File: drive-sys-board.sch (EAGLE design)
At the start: 34 parts

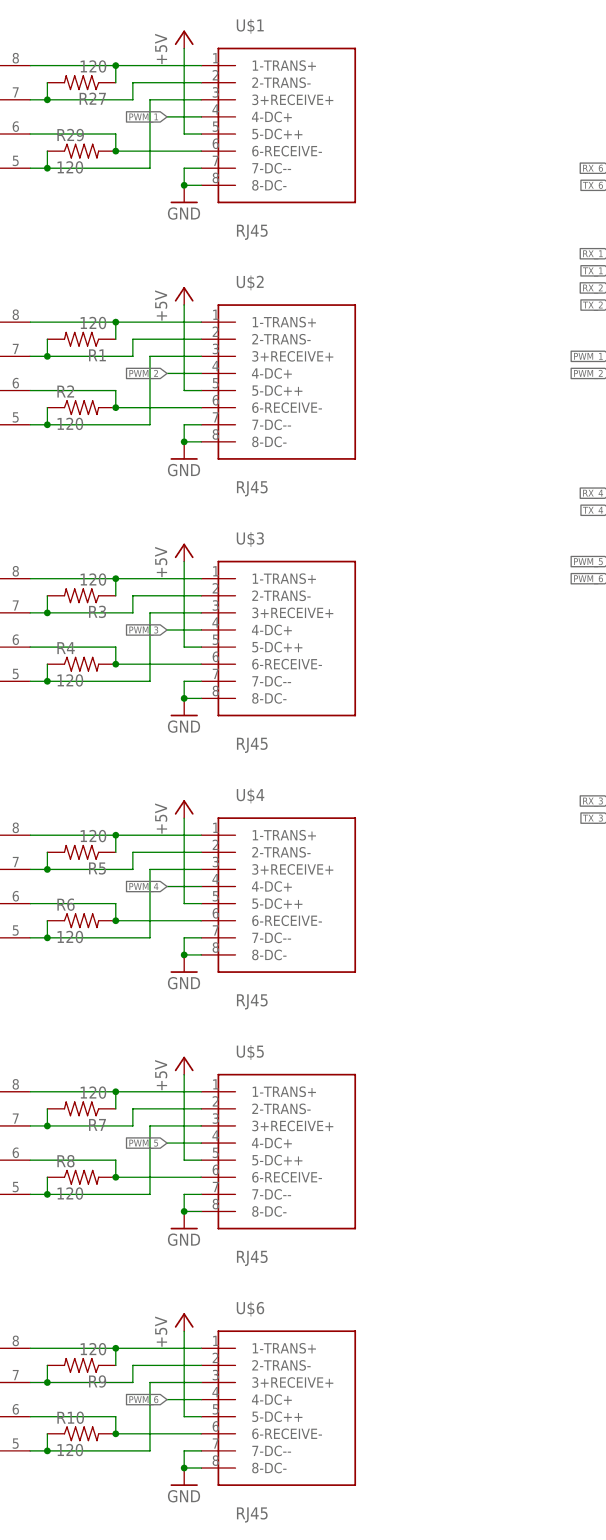
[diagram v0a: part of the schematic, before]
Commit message: changed rj45 conn
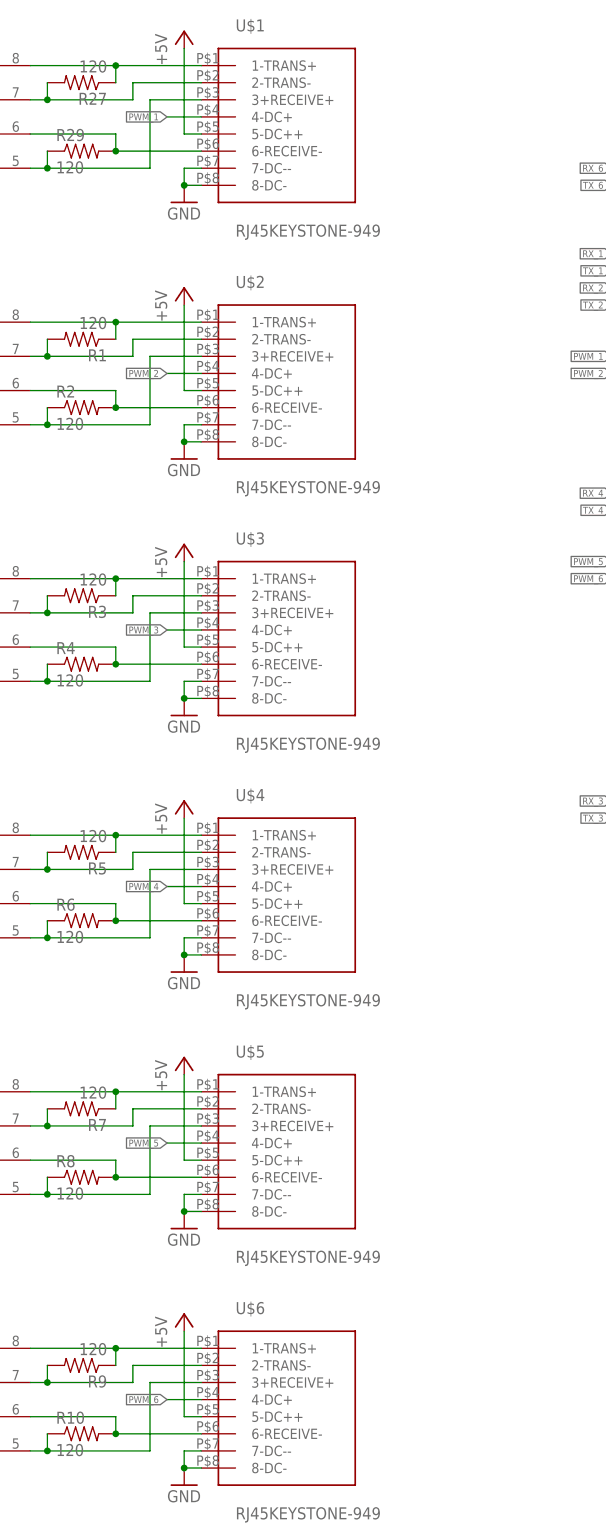
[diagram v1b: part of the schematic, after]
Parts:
- U$1, U$2, U$3, U$4, U$5, U$6: value RJ45 -> RJ45KEYSTONE-949; device MRDT-2014-All:RJ45 -> MRDT-2015-General:RJ45KEYSTONE-949
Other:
- moved on the sheet: U$1, U$2, U$3, U$4, U$5, U$6
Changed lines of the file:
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@@
 <part name="C1" library="SparkFun-Passives" deviceset="CAP" device="1206" value="0.1uF"/>
 <part name="GND13" library="supply1" deviceset="GND" device=""/>
-<part name="U$1" library="MRDT-2014-All" deviceset="RJ45" device=""/>
+<part name="U$1" library="MRDT-2015-General" deviceset="RJ45" device="KEYSTONE-949" value="RJ45KEYSTONE-949"/>
 <part name="GND1" library="supply1" deviceset="GND" device=""/>
 <part name="P+1" library="supply1" deviceset="+5V" device=""/>
@@
 <part name="C2" library="SparkFun-Passives" deviceset="CAP" device="1206" value="0.1uF"/>
 <part name="GND3" library="supply1" deviceset="GND" device=""/>
-<part name="U$2" library="MRDT-2014-All" deviceset="RJ45" device=""/>
+<part name="U$2" library="MRDT-2015-General" deviceset="RJ45" device="KEYSTONE-949"/>
 <part name="GND4" library="supply1" deviceset="GND" device=""/>
 <part name="P+3" library="supply1" deviceset="+5V" device=""/>
@@
 <part name="C3" library="SparkFun-Passives" deviceset="CAP" device="1206" value="0.1uF"/>
 <part name="GND6" library="supply1" deviceset="GND" device=""/>
-<part name="U$3" library="MRDT-2014-All" deviceset="RJ45" device=""/>
+<part name="U$3" library="MRDT-2015-General" deviceset="RJ45" device="KEYSTONE-949"/>
 <part name="GND7" library="supply1" deviceset="GND" device=""/>
 <part name="P+5" library="supply1" deviceset="+5V" device=""/>
@@
 <part name="C4" library="SparkFun-Passives" deviceset="CAP" device="1206" value="0.1uF"/>
 <part name="GND9" library="supply1" deviceset="GND" device=""/>
-<part name="U$4" library="MRDT-2014-All" deviceset="RJ45" device=""/>
+<part name="U$4" library="MRDT-2015-General" deviceset="RJ45" device="KEYSTONE-949"/>
 <part name="GND10" library="supply1" deviceset="GND" device=""/>
 <part name="P+7" library="supply1" deviceset="+5V" device=""/>
@@
 <part name="C5" library="SparkFun-Passives" deviceset="CAP" device="1206" value="0.1uF"/>
 <part name="GND14" library="supply1" deviceset="GND" device=""/>
-<part name="U$5" library="MRDT-2014-All" deviceset="RJ45" device=""/>
+<part name="U$5" library="MRDT-2015-General" deviceset="RJ45" device="KEYSTONE-949"/>
 <part name="GND15" library="supply1" deviceset="GND" device=""/>
 <part name="P+9" library="supply1" deviceset="+5V" device=""/>
@@
 <part name="C6" library="SparkFun-Passives" deviceset="CAP" device="1206" value="0.1uF"/>
 <part name="GND17" library="supply1" deviceset="GND" device=""/>
-<part name="U$6" library="MRDT-2014-All" deviceset="RJ45" device=""/>
+<part name="U$6" library="MRDT-2015-General" deviceset="RJ45" device="KEYSTONE-949"/>
 <part name="GND18" library="supply1" deviceset="GND" device=""/>
 <part name="P+11" library="supply1" deviceset="+5V" device=""/>

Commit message: finalized board
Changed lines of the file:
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@@
 <part name="H1" library="holes" deviceset="MOUNT-HOLE" device="3.2"/>
 <part name="U$7" library="MRDT-2015-General" deviceset="MLX-3-PIN" device=""/>
-<part name="U$8" library="MRDT-2015-General" deviceset="MRDT_LOGO" device=""/>
 <part name="U$10" library="MRDT-2015-General" deviceset="MAX3077" device=""/>
 <part name="U$11" library="MRDT-2015-General" deviceset="MAX3077" device=""/>
@@
 <part name="U$15" library="MRDT-2015-General" deviceset="MAX3077" device=""/>
 <part name="GND12" library="supply1" deviceset="GND" device=""/>
+<part name="U$8" library="MRDT-2015-General" deviceset="MRDT_LOGO" device=""/>
 </parts>
 <sheets>
@@
 <instance part="H1" gate="G$1" x="-5.08" y="-27.94"/>
 <instance part="U$7" gate="G$1" x="88.9" y="114.3"/>
-<instance part="U$8" gate="G$1" x="68.58" y="0"/>
 <instance part="U$10" gate="G$1" x="-101.6" y="106.68"/>
 <instance part="U$11" gate="G$1" x="-101.6" y="68.58"/>
@@
 <instance part="U$15" gate="G$1" x="-101.6" y="-83.82"/>
 <instance part="GND12" gate="1" x="-127" y="106.68"/>
+<instance part="U$8" gate="G$1" x="63.5" y="2.54"/>
 </instances>
 <busses>
@@
 </sheet>
 </sheets>
+<errors>
+</errors>
 </schematic>
 </drawing>

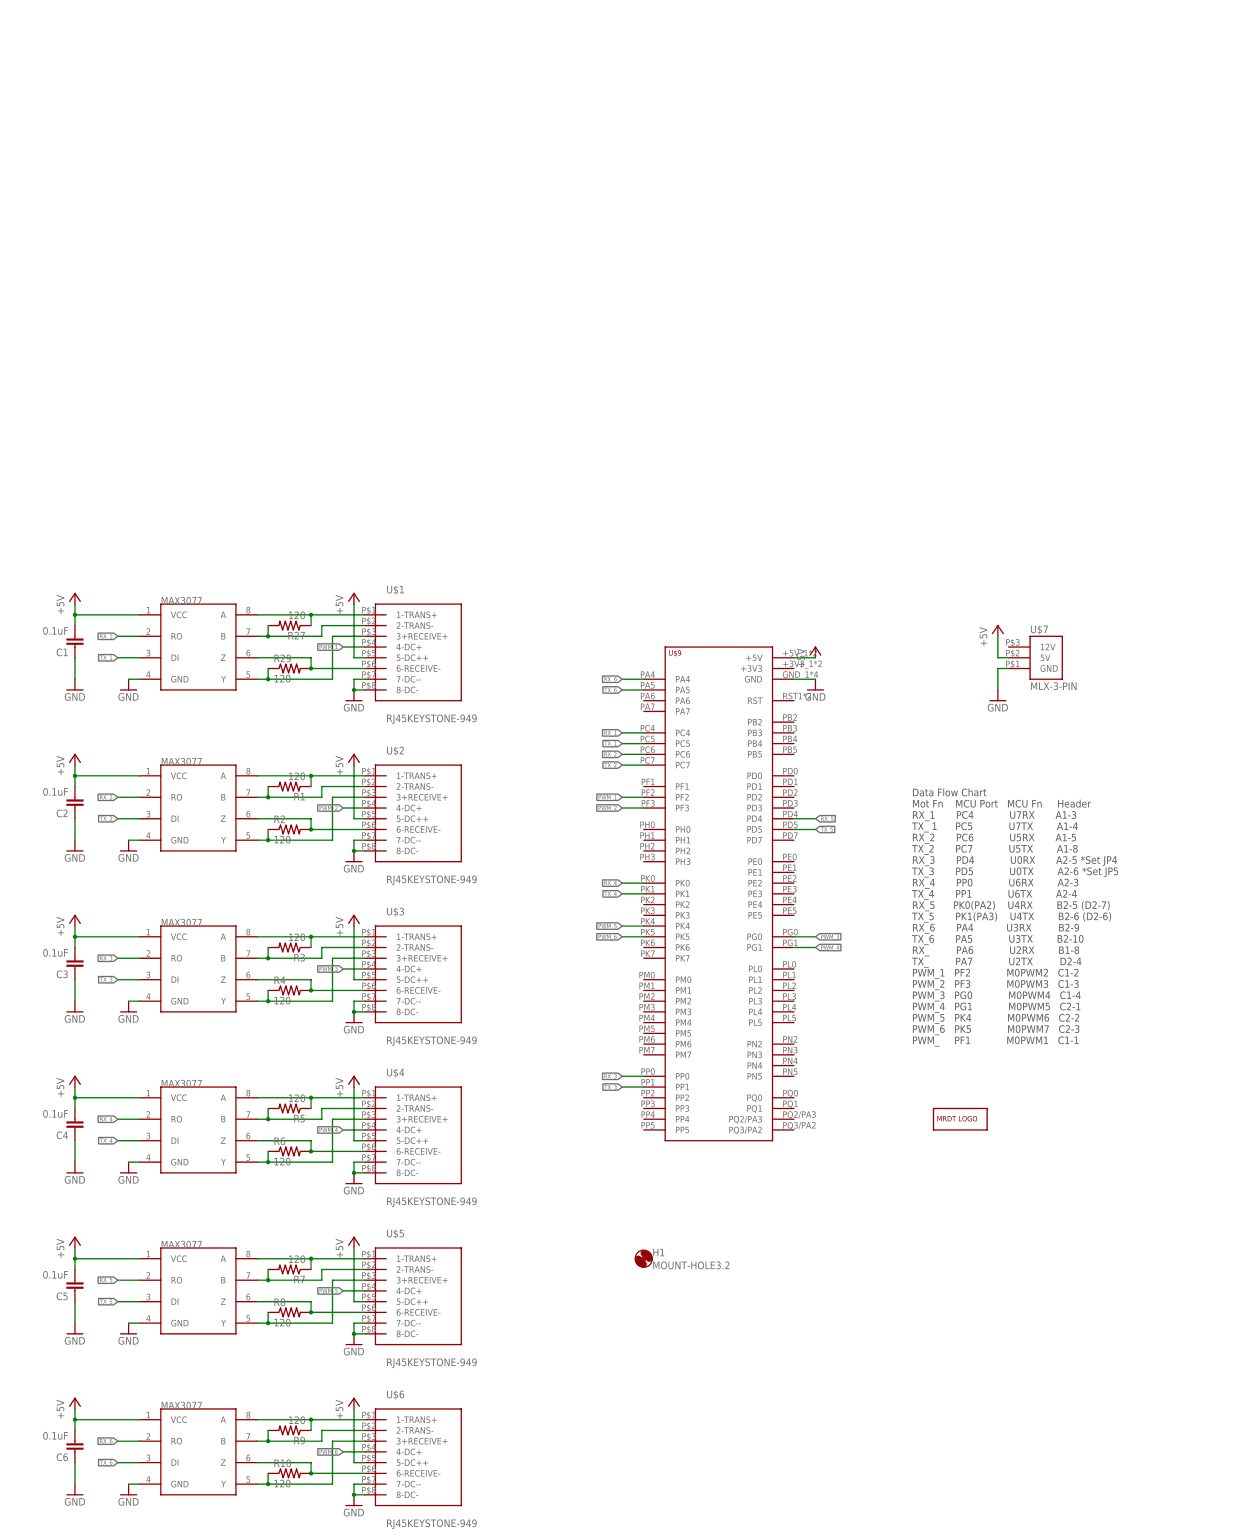
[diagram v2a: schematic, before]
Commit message: finished rs232 drive board
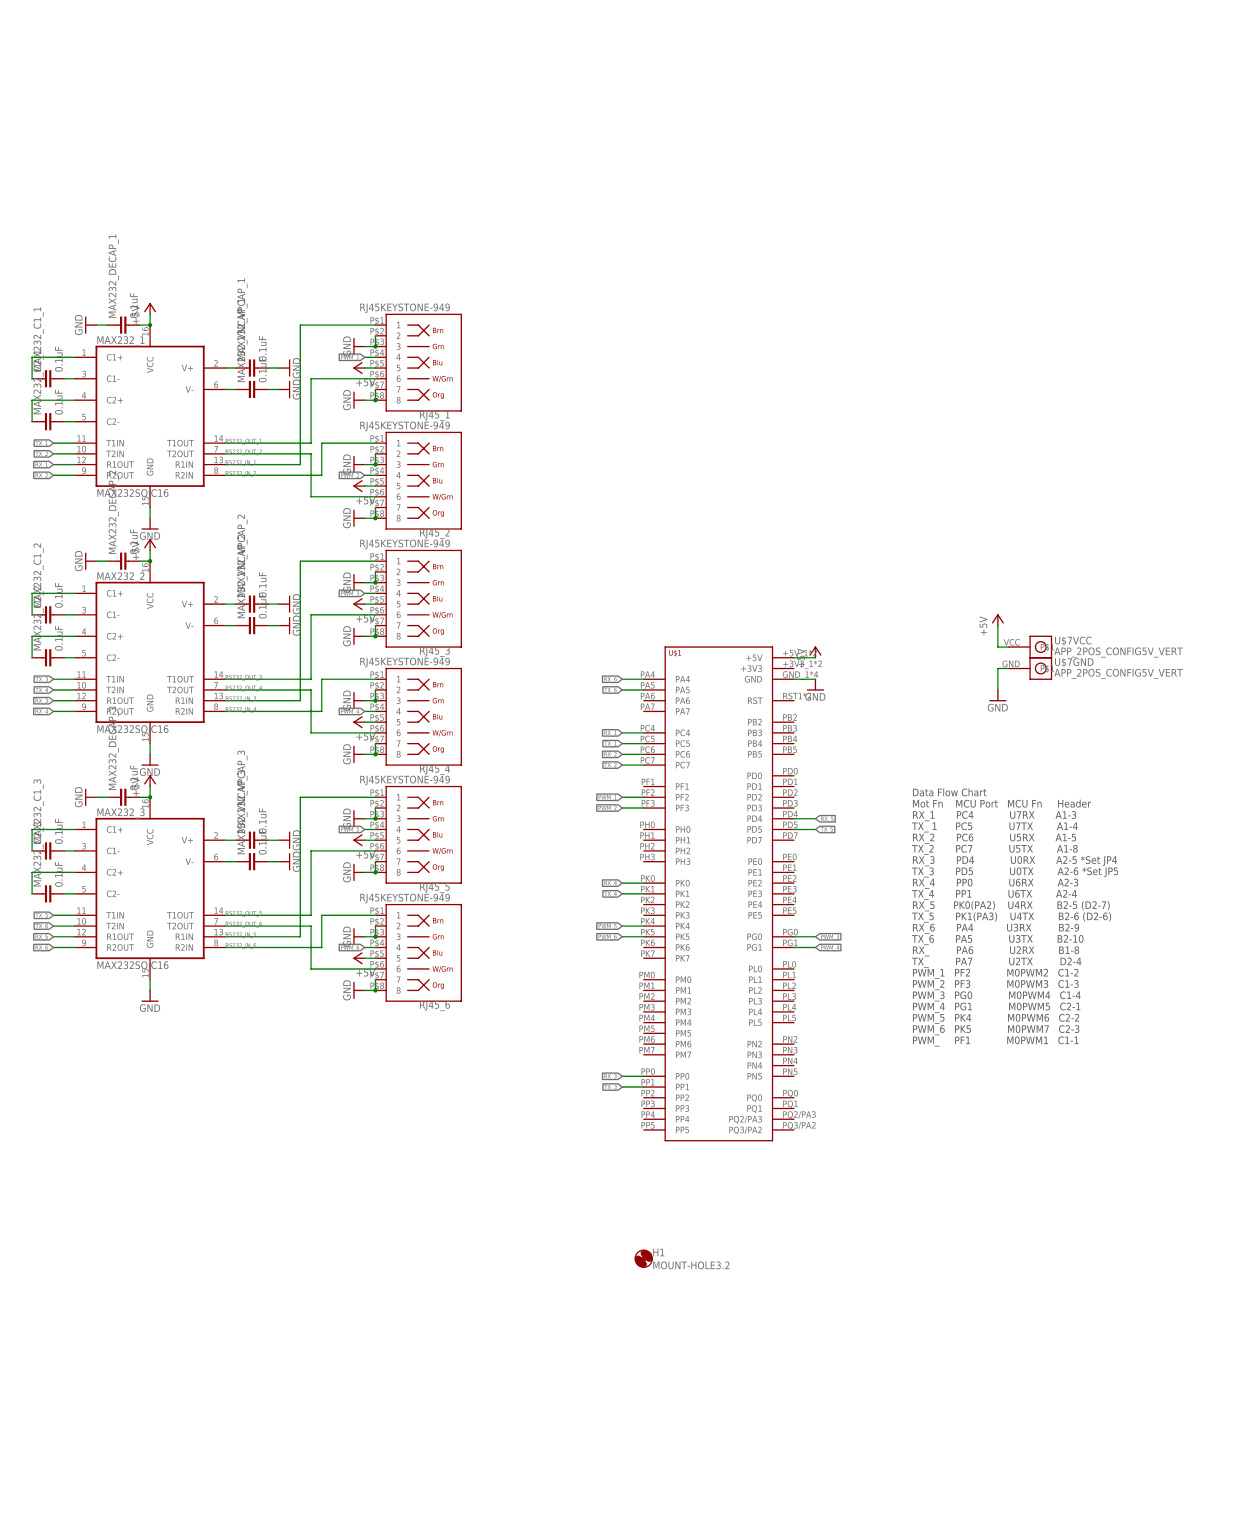
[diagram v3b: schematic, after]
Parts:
- removed C1, C2, C3, C4, C5, C6: 0.1uF, SparkFun-Passives:CAP1206
- removed R1, R10, R2, R27, R29, R3, R4, R5, R6, R7, R8, R9: 120, SparkFun-Passives:RESISTOR1206
- removed U$10, U$11, U$12, U$13, U$14, U$15: MAX3077, MRDT-2015-General:MAX3077
- removed U$2, U$3, U$4, U$5, U$6: RJ45KEYSTONE-949, MRDT-2015-General:RJ45KEYSTONE-949
- removed U$8: MRDT_LOGO, MRDT-2015-General:MRDT_LOGO
- removed U$9: TIVA-C-CONNECTED, MRDT-2015-General:TIVA-C-CONNECTED
- added MAX232_1, MAX232_2, MAX232_3: MAX232SOIC16, SparkFun-DigitalIC:MAX232SOIC16
- added MAX232_C1_1, MAX232_C1_2, MAX232_C1_3, MAX232_C2_1, MAX232_C2_2, MAX232_C2_3, MAX232_DECAP_1, MAX232_DECAP_2, MAX232_DECAP_3, MAX232_VNCAP_1, MAX232_VNCAP_2, MAX232_VNCAP_3, MAX232_VPCAP_1, MAX232_VPCAP_2, MAX232_VPCAP_3: 0.1uF, SparkFun-Capacitors:CAP1206
- added RJ45_1, RJ45_2, RJ45_3, RJ45_4, RJ45_5, RJ45_6: RJ45KEYSTONE-949, MRDT-2015-General:RJ45KEYSTONE-949
- U$1: value RJ45KEYSTONE-949 -> TIVA-C-CONNECTED; device MRDT-2015-General:RJ45KEYSTONE-949 -> MRDT-2015-General:TIVA-C-CONNECTED
- U$7: value MLX-3-PIN -> APP_2POS_CONFIG5V_VERT; device MRDT-2015-General:MLX-3-PIN -> MRDT-Connectors:APP_2POS_CONFIG5V_VERT
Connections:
- removed net 18_RX+: R27.1, U$1.1-TRANS+, U$10.A
- removed net 18_RX+1: R1.1, U$11.A, U$2.1-TRANS+
- removed net 18_RX+2: R3.1, U$12.A, U$3.1-TRANS+
- removed net 18_RX+3: R5.1, U$13.A, U$4.1-TRANS+
- removed net 18_RX+4: R7.1, U$14.A, U$5.1-TRANS+
- removed net 18_RX+5: R9.1, U$15.A, U$6.1-TRANS+
- removed net 18_RX-: R27.2, U$1.2-TRANS-, U$10.B
- removed net 18_RX-1: R1.2, U$11.B, U$2.2-TRANS-
- removed net 18_RX-2: R3.2, U$12.B, U$3.2-TRANS-
- removed net 18_RX-3: R5.2, U$13.B, U$4.2-TRANS-
- removed net 18_RX-4: R7.2, U$14.B, U$5.2-TRANS-
- removed net 18_RX-5: R9.2, U$15.B, U$6.2-TRANS-
- removed net 18_TX+: R29.1, U$1.3+RECEIVE+, U$10.Y
- removed net 18_TX+1: R2.1, U$11.Y, U$2.3+RECEIVE+
- removed net 18_TX+2: R4.1, U$12.Y, U$3.3+RECEIVE+
- removed net 18_TX+3: R6.1, U$13.Y, U$4.3+RECEIVE+
- removed net 18_TX+4: R8.1, U$14.Y, U$5.3+RECEIVE+
- removed net 18_TX+5: R10.1, U$15.Y, U$6.3+RECEIVE+
- removed net 18_TX-: R29.2, U$1.6-RECEIVE-, U$10.Z
- removed net 18_TX-1: R2.2, U$11.Z, U$2.6-RECEIVE-
- removed net 18_TX-2: R4.2, U$12.Z, U$3.6-RECEIVE-
- removed net 18_TX-3: R6.2, U$13.Z, U$4.6-RECEIVE-
- removed net 18_TX-4: R8.2, U$14.Z, U$5.6-RECEIVE-
- removed net 18_TX-5: R10.2, U$15.Z, U$6.6-RECEIVE-
- new net N$1_1: MAX232_1.C1+, MAX232_C1_1.1
- new net N$1_2: MAX232_2.C1+, MAX232_C1_2.1
- new net N$1_3: MAX232_3.C1+, MAX232_C1_3.1
- new net N$2_1: MAX232_1.V+, MAX232_VPCAP_1.1
- new net N$2_2: MAX232_2.V+, MAX232_VPCAP_2.1
- new net N$2_3: MAX232_3.V+, MAX232_VPCAP_3.1
- new net N$3_1: MAX232_1.C1-, MAX232_C1_1.2
- new net N$3_2: MAX232_2.C1-, MAX232_C1_2.2
- new net N$3_3: MAX232_3.C1-, MAX232_C1_3.2
- new net N$4_1: MAX232_1.C2+, MAX232_C2_1.1
- new net N$4_2: MAX232_2.C2+, MAX232_C2_2.1
- new net N$4_3: MAX232_3.C2+, MAX232_C2_3.1
- new net N$5_1: MAX232_1.C2-, MAX232_C2_1.2
- new net N$5_2: MAX232_2.C2-, MAX232_C2_2.2
- new net N$5_3: MAX232_3.C2-, MAX232_C2_3.2
- new net N$6_1: MAX232_1.V-, MAX232_VNCAP_1.1
- new net N$6_2: MAX232_2.V-, MAX232_VNCAP_2.1
- new net N$6_3: MAX232_3.V-, MAX232_VNCAP_3.1
- new net RS232_IN_1: MAX232_1.R1IN, RJ45_1.1
- new net RS232_IN_2: MAX232_1.R2IN, RJ45_2.1
- new net RS232_IN_3: MAX232_2.R1IN, RJ45_3.1
- new net RS232_IN_4: MAX232_2.R2IN, RJ45_4.1
- new net RS232_IN_5: MAX232_3.R1IN, RJ45_5.1
- new net RS232_IN_6: MAX232_3.R2IN, RJ45_6.1
- new net RS232_OUT_1: MAX232_1.T1OUT, RJ45_1.6
- new net RS232_OUT_2: MAX232_1.T2OUT, RJ45_2.6
- new net RS232_OUT_3: MAX232_2.T1OUT, RJ45_3.6
- new net RS232_OUT_4: MAX232_2.T2OUT, RJ45_4.6
- new net RS232_OUT_5: MAX232_3.T1OUT, RJ45_5.6
- new net RS232_OUT_6: MAX232_3.T2OUT, RJ45_6.6
- net +5V: now also MAX232_1.VCC, MAX232_2.VCC, MAX232_3.VCC, MAX232_DECAP_1.2, MAX232_DECAP_2.2, MAX232_DECAP_3.2, RJ45_1.5, RJ45_2.5, RJ45_3.5, RJ45_4.5, RJ45_5.5, RJ45_6.5, U$1.+5V, U$7VCC.P$1; no longer C1.2, C2.2, C3.2, C4.2, C5.2, C6.2, U$1.5-DC++, U$10.VCC, U$11.VCC, U$12.VCC, U$13.VCC, U$14.VCC, U$15.VCC, U$2.5-DC++, U$3.5-DC++, U$4.5-DC++, U$5.5-DC++, U$6.5-DC++, U$7.5V, U$9.+5V
- net GND: now also MAX232_1.GND, MAX232_2.GND, MAX232_3.GND, MAX232_DECAP_1.1, MAX232_DECAP_2.1, MAX232_DECAP_3.1, MAX232_VNCAP_1.2, MAX232_VNCAP_2.2, MAX232_VNCAP_3.2, MAX232_VPCAP_1.2, MAX232_VPCAP_2.2, MAX232_VPCAP_3.2, RJ45_1.2, RJ45_1.3, RJ45_1.7, RJ45_1.8, RJ45_2.2, RJ45_2.3, RJ45_2.7, RJ45_2.8, RJ45_3.2, RJ45_3.3, RJ45_3.7, RJ45_3.8, RJ45_4.2, RJ45_4.3, RJ45_4.7, RJ45_4.8, RJ45_5.2, RJ45_5.3, RJ45_5.7, RJ45_5.8, RJ45_6.2, RJ45_6.3, RJ45_6.7, RJ45_6.8, U$1.GND, U$7GND.P$1; no longer C1.1, C2.1, C3.1, C4.1, C5.1, C6.1, U$1.7-DC--, U$1.8-DC-, U$10.GND, U$11.GND, U$12.GND, U$13.GND, U$14.GND, U$15.GND, U$2.7-DC--, U$2.8-DC-, U$3.7-DC--, U$3.8-DC-, U$4.7-DC--, U$4.8-DC-, U$5.7-DC--, U$5.8-DC-, U$6.7-DC--, U$6.8-DC-, U$7.GND, U$9.GND
- net PWM_1: now also RJ45_1.4, U$1.PF2; no longer U$1.4-DC+, U$9.PF2
- net PWM_2: now also RJ45_2.4, U$1.PF3; no longer U$2.4-DC+, U$9.PF3
- net PWM_3: now also RJ45_3.4, U$1.PG0; no longer U$3.4-DC+, U$9.PG0
- net PWM_4: now also RJ45_4.4, U$1.PG1; no longer U$4.4-DC+, U$9.PG1
- net PWM_5: now also RJ45_5.4, U$1.PK4; no longer U$5.4-DC+, U$9.PK4
- net PWM_6: now also RJ45_6.4, U$1.PK5; no longer U$6.4-DC+, U$9.PK5
- net RX_1: now also MAX232_1.R1OUT, U$1.PC4; no longer U$10.RO, U$9.PC4
- net RX_2: now also MAX232_1.R2OUT, U$1.PC6; no longer U$11.RO, U$9.PC6
- net RX_3: now also MAX232_2.R1OUT, U$1.PP0; no longer U$12.RO, U$9.PP0
- net RX_4: now also MAX232_2.R2OUT, U$1.PK0; no longer U$13.RO, U$9.PK0
- net RX_5: now also MAX232_3.R1OUT, U$1.PD4; no longer U$14.RO, U$9.PD4
- net RX_6: now also MAX232_3.R2OUT, U$1.PA4; no longer U$15.RO, U$9.PA4
- net TX_1: now also MAX232_1.T1IN, U$1.PC5; no longer U$10.DI, U$9.PC5
- net TX_2: now also MAX232_1.T2IN, U$1.PC7; no longer U$11.DI, U$9.PC7
- net TX_3: now also MAX232_2.T1IN, U$1.PP1; no longer U$12.DI, U$9.PP1
- net TX_4: now also MAX232_2.T2IN, U$1.PK1; no longer U$13.DI, U$9.PK1
- net TX_5: now also MAX232_3.T1IN, U$1.PD5; no longer U$14.DI, U$9.PD5
- net TX_6: now also MAX232_3.T2IN, U$1.PA5; no longer U$15.DI, U$9.PA5
